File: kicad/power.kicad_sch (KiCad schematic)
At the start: 50 parts, among them J1 Bus_PCI_Express_x1, J2 wago 2060-452/998-404, J3 wago 2060-452/998-404, J4 Conn_01x04, J5 Conn_01x02_Pin, J6 USB_C_Receptacle_USB2.0_16P, Q1 SI7232DN-T1-GE3, U2 RP2040, U4 W25Q128JVP, U9 MCP25625T-E/ML, X1 RP2040 Crystal, Y2 X322516MLB4SI

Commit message: add hierarchical sheets
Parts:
- removed C1: 100u, Capacitor_SMD:C_1210_3225Metric, symbol Device:C
- removed C10, C11: 15p, Capacitor_SMD:C_0402_1005Metric, symbol Device:C
- removed C206, C207, C209, C211, C212, C213, C214, C215, C216, C40, C90, C92, C93: 100n, Capacitor_SMD:C_0402_1005Metric, symbol Device:C
- removed C208, C210: 1u, Capacitor_SMD:C_0402_1005Metric, symbol Device:C
- removed C94, C95: 22p, Capacitor_SMD:C_0402_1005Metric, symbol Device:C
- removed J2, J3: wago 2060-452/998-404, 4in-recovery:wago-2060-452_998-404, symbol recovery:wago-2060-452_998-404
- removed J4: Conn_01x04, Connector_PinHeader_2.54mm:PinHeader_1x04_P2.54mm_Vertical, symbol Connector_Generic:Conn_01x04
- removed J5: Conn_01x02_Pin, Connector_PinHeader_2.54mm:PinHeader_1x02_P2.54mm_Vertical, symbol Connector:Conn_01x02_Pin
- removed Q1: SI7232DN-T1-GE3, 4in-recovery:SI7232DN-T1-GE3, symbol 4in-recovery:SI7232DN-T1-GE3
- removed R12, R30: 1k, Resistor_SMD:R_0402_1005Metric, symbol Device:R
- removed R20, R300: 100, Resistor_SMD:R_0402_1005Metric, symbol Device:R
- removed R203, R204: 27, Resistor_SMD:R_0402_1005Metric, symbol Device:R
- removed R21, R31: 3.3k, Resistor_SMD:R_0402_1005Metric, symbol Device:R
- removed R22, R32: 100k, Resistor_SMD:R_0402_1005Metric, symbol Device:R
- removed R23, R33: 27k, Resistor_SMD:R_0402_1005Metric, symbol Device:R
- removed R91: 10k, Resistor_SMD:R_0402_1005Metric, symbol Device:R
- removed S2: TS-1187A-B-A-B, 4in-kicad-library:TS-1187A-B-A-B, symbol 4in-kicad-library:TS-1187A-B-A-B
- removed U2: RP2040, Package_DFN_QFN:QFN-56-1EP_7x7mm_P0.4mm_EP3.2x3.2mm, symbol MCU_RaspberryPi:RP2040
- removed U4: W25Q128JVP, Package_SON:WSON-8-1EP_6x5mm_P1.27mm_EP3.4x4.3mm, symbol Memory_Flash:W25Q128JVP
- removed U9: MCP25625T-E/ML, 4in-kicad-library:QFN28_6X6MC_MCH, symbol 4in-kicad-library:MCP25625T-E_ML
- removed X1: RP2040 Crystal, 4in-kicad-library:ABM8-272-T3_ABR, symbol 4in-kicad-library:ABM8-272-T3
- removed Y2: X322516MLB4SI, 4in-kicad-library:X322516MLB4SI, symbol 4in-kicad-library:X322516MLB4SI
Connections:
- net VBUS: now reaches J6.A4 (VBUS), J6.A9 (VBUS), J6.B4 (VBUS), J6.B9 (VBUS)
- removed net v_lipo: J1.A16 (VBAT), J1.A17 (VBAT), J1.A18 (VBAT), J1.B16 (VBAT), J1.B17 (VBAT), J1.B18 (VBAT)
- no-connect marks 34 -> 13
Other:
- added sheet digital (digital.kicad_sch)
- added sheet power (analog.kicad_sch)
- note added: "Power Module 0.1.0"
- note removed: "CAN"
- note removed: "CAN Controller/Tranceiver"
- note removed: "Flash"
- note removed: "MCU"
- note removed: "Make sure C210 is close to pin 44 of RP2040"
- note removed: "Make sure C8 is close to pin 45 of RP2040"
- note removed: "Make sure R3 and R4 are close to RP2040"
- note removed: "Parachute Circuit"
- note removed: "RP2040 Crystal"
- note removed: "Recovery Module 0.1.0"
- note removed: "USB Boot shorting headders"
- moved on the sheet: D1, J1, J6, R2, R3, R4

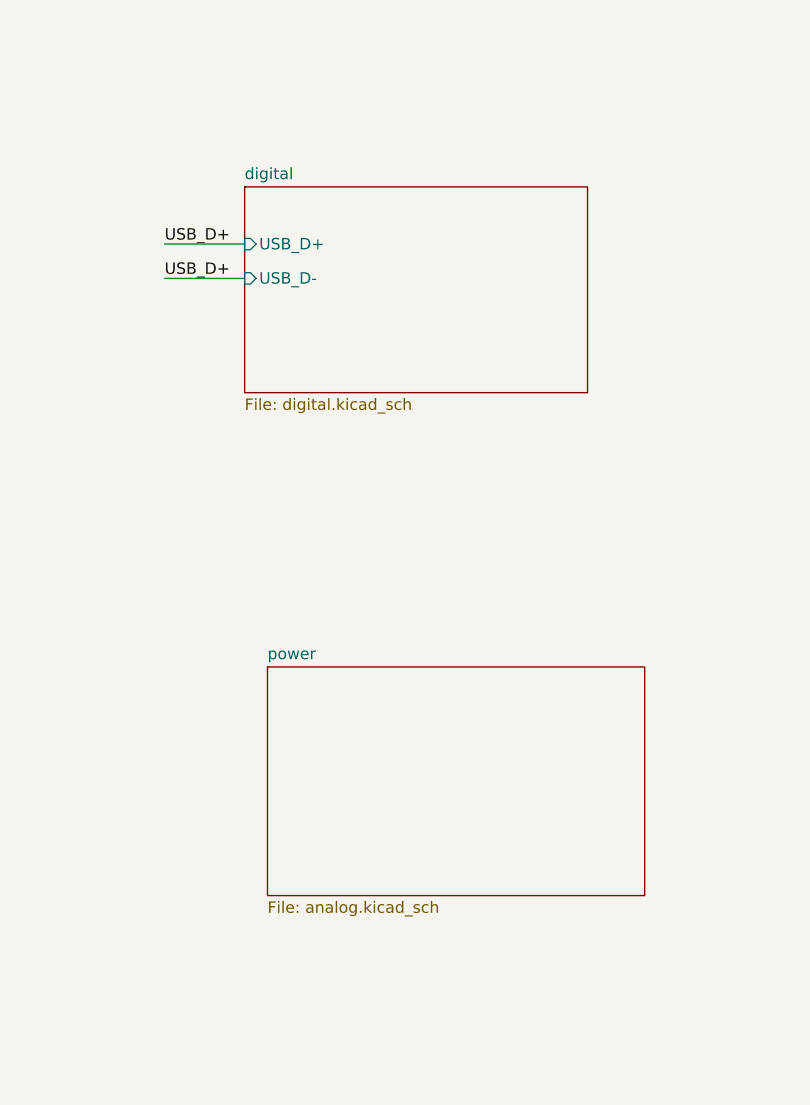
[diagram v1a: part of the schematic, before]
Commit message: add charging/balancing IC to library
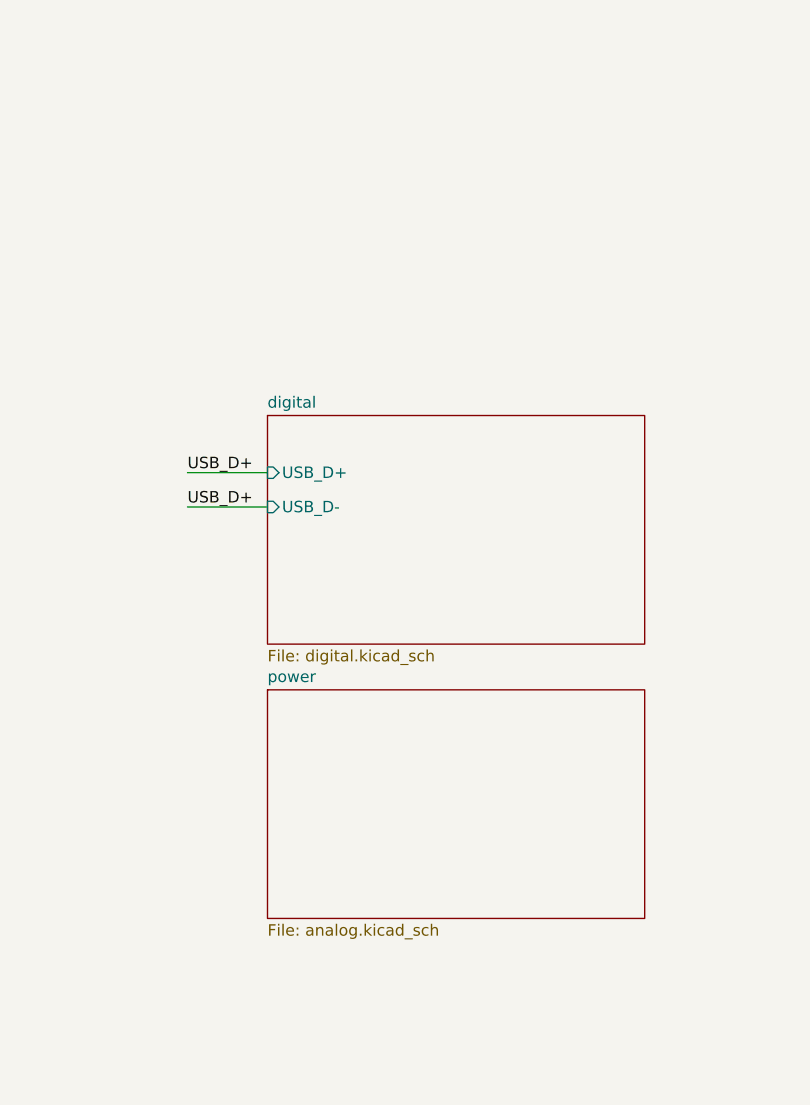
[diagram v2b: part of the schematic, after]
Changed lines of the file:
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@@
+	(wire
+		(pts
+			(xy 199.39 78.74) (xy 208.28 78.74)
+		)
+		(stroke
+			(width 0)
+			(type default)
+		)
+	)
 	(wire
 		(pts
@@
 	(wire
 		(pts
-			(xy 196.85 53.34) (xy 205.74 53.34)
+			(xy 121.92 135.89) (xy 121.92 130.81)
 		)
 		(stroke
@@
 	(wire
 		(pts
-			(xy 121.92 135.89) (xy 121.92 130.81)
+			(xy 121.92 100.33) (xy 121.92 105.41)
 		)
 		(stroke
@@
 	(wire
 		(pts
-			(xy 121.92 100.33) (xy 121.92 105.41)
+			(xy 91.44 105.41) (xy 91.44 110.49)
 		)
 		(stroke
@@
 	(wire
 		(pts
-			(xy 91.44 105.41) (xy 91.44 110.49)
+			(xy 121.92 115.57) (xy 121.92 120.65)
 		)
 		(stroke
@@
 	(wire
 		(pts
-			(xy 121.92 115.57) (xy 121.92 120.65)
+			(xy 91.44 135.89) (xy 91.44 140.97)
 		)
 		(stroke
@@
 	(wire
 		(pts
-			(xy 91.44 135.89) (xy 91.44 140.97)
+			(xy 86.36 156.21) (xy 91.44 156.21)
 		)
 		(stroke
@@
 	(wire
 		(pts
-			(xy 86.36 156.21) (xy 91.44 156.21)
+			(xy 86.36 135.89) (xy 91.44 135.89)
 		)
 		(stroke
@@
 	(wire
 		(pts
-			(xy 86.36 135.89) (xy 91.44 135.89)
+			(xy 127 135.89) (xy 121.92 135.89)
 		)
 		(stroke
@@
 	(wire
 		(pts
-			(xy 127 135.89) (xy 121.92 135.89)
+			(xy 121.92 110.49) (xy 121.92 115.57)
 		)
 		(stroke
@@
 	(wire
 		(pts
-			(xy 121.92 110.49) (xy 121.92 115.57)
+			(xy 91.44 156.21) (xy 91.44 161.29)
 		)
 		(stroke
@@
 	(wire
 		(pts
-			(xy 91.44 156.21) (xy 91.44 161.29)
+			(xy 54.61 55.88) (xy 54.61 58.42)
 		)
 		(stroke
@@
 	(wire
 		(pts
-			(xy 54.61 55.88) (xy 54.61 58.42)
+			(xy 199.39 74.93) (xy 208.28 74.93)
 		)
 		(stroke
@@
 		(pts
 			(xy 127 156.21) (xy 121.92 156.21)
-		)
-		(stroke
-			(width 0)
-			(type default)
-		)
-	)
-	(wire
-		(pts
-			(xy 196.85 49.53) (xy 205.74 49.53)
 		)
 		(stroke
@@
 	)
 	(label "USB_D+"
-		(at 196.85 49.53 0)
+		(at 199.39 74.93 0)
 		(effects
 			(font
@@
 	)
 	(label "USB_D+"
-		(at 196.85 53.34 0)
+		(at 199.39 78.74 0)
 		(effects
 			(font
@@
 	)
 	(sheet
-		(at 205.74 43.18)
-		(size 38.1 22.86)
-		(exclude_from_sim no)
-		(in_bom yes)
-		(on_board yes)
-		(dnp no)
-		(fields_autoplaced yes)
-		(stroke
-			(width 0.1524)
-			(type solid)
-		)
-		(fill
-			(color 0 0 0 0.0000)
-		)
-		(property "Sheetname" "digital"
-			(at 205.74 42.4684 0)
-			(effects
-				(font
-					(size 1.27 1.27)
-				)
-				(justify left bottom)
-			)
-		)
-		(property "Sheetfile" "digital.kicad_sch"
-			(at 205.74 66.6246 0)
-			(effects
-				(font
-					(size 1.27 1.27)
-				)
-				(justify left top)
-			)
-		)
-		(pin "USB_D+" input
-			(at 205.74 49.53 180)
-			(effects
-				(font
-					(size 1.27 1.27)
-				)
-				(justify left)
-			)
-		)
-		(pin "USB_D-" input
-			(at 205.74 53.34 180)
-			(effects
-				(font
-					(size 1.27 1.27)
-				)
-				(justify left)
-			)
-		)
-		(instances
-			(project "power"
-				(path "/612ece3f-e722-4b33-8111-645d24cfcf05"
-					(page "2")
-				)
-			)
-		)
-	)
-	(sheet
-		(at 208.28 96.52)
+		(at 208.28 68.58)
 		(size 41.91 25.4)
 		(exclude_from_sim no)
@@
 			(color 0 0 0 0.0000)
 		)
+		(property "Sheetname" "digital"
+			(at 208.28 67.8684 0)
+			(effects
+				(font
+					(size 1.27 1.27)
+				)
+				(justify left bottom)
+			)
+		)
+		(property "Sheetfile" "digital.kicad_sch"
+			(at 208.28 94.5646 0)
+			(effects
+				(font
+					(size 1.27 1.27)
+				)
+				(justify left top)
+			)
+		)
+		(pin "USB_D+" input
+			(at 208.28 74.93 180)
+			(effects
+				(font
+					(size 1.27 1.27)
+				)
+				(justify left)
+			)
+		)
+		(pin "USB_D-" input
+			(at 208.28 78.74 180)
+			(effects
+				(font
+					(size 1.27 1.27)
+				)
+				(justify left)
+			)
+		)
+		(instances
+			(project "power"
+				(path "/612ece3f-e722-4b33-8111-645d24cfcf05"
+					(page "2")
+				)
+			)
+		)
+	)
+	(sheet
+		(at 208.28 99.06)
+		(size 41.91 25.4)
+		(exclude_from_sim no)
+		(in_bom yes)
+		(on_board yes)
+		(dnp no)
+		(fields_autoplaced yes)
+		(stroke
+			(width 0.1524)
+			(type solid)
+		)
+		(fill
+			(color 0 0 0 0.0000)
+		)
 		(property "Sheetname" "power"
-			(at 208.28 95.8084 0)
+			(at 208.28 98.3484 0)
 			(effects
 				(font
@@
 		)
 		(property "Sheetfile" "analog.kicad_sch"
-			(at 208.28 122.5046 0)
-			(effects
-				(font
+			(at 208.28 125.0446 0)
+			(effects
+				(font

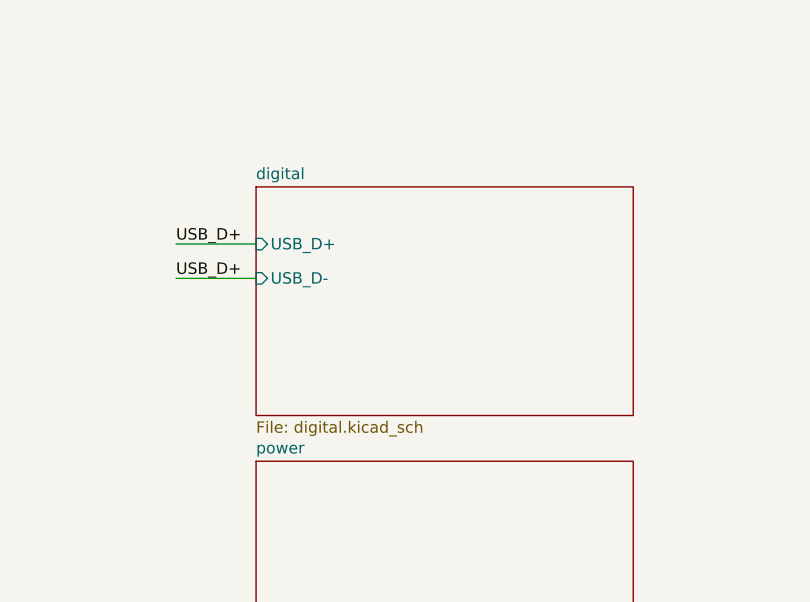
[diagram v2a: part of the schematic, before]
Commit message: update library schmatic for balancing IC
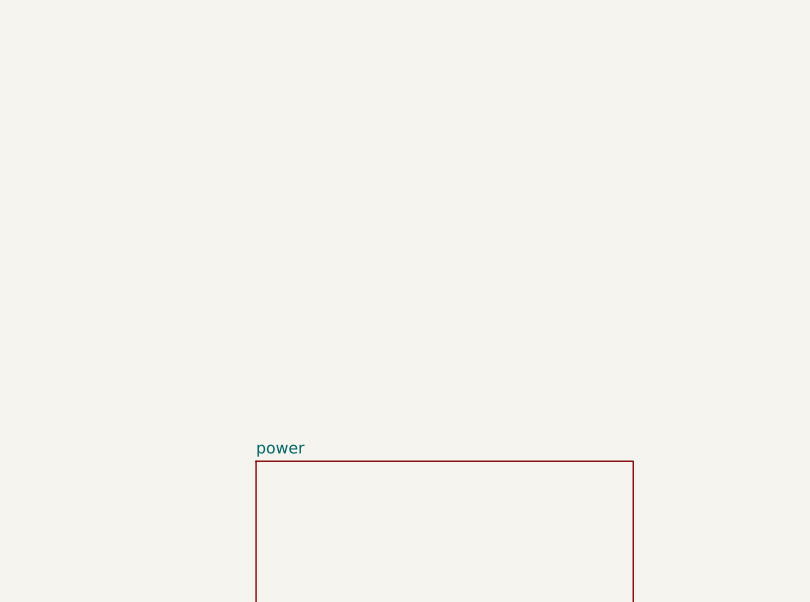
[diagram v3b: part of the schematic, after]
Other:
- removed sheet digital
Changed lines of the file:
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@@
 	(wire
 		(pts
-			(xy 199.39 78.74) (xy 208.28 78.74)
+			(xy 91.44 110.49) (xy 91.44 115.57)
 		)
 		(stroke
@@
 	(wire
 		(pts
-			(xy 91.44 110.49) (xy 91.44 115.57)
+			(xy 121.92 105.41) (xy 121.92 110.49)
 		)
 		(stroke
@@
 	(wire
 		(pts
-			(xy 121.92 105.41) (xy 121.92 110.49)
+			(xy 54.61 53.34) (xy 54.61 50.8)
 		)
 		(stroke
@@
 	(wire
 		(pts
-			(xy 54.61 53.34) (xy 54.61 50.8)
+			(xy 121.92 156.21) (xy 121.92 151.13)
 		)
 		(stroke
@@
 	(wire
 		(pts
-			(xy 121.92 156.21) (xy 121.92 151.13)
+			(xy 91.44 135.89) (xy 91.44 130.81)
 		)
 		(stroke
@@
 	(wire
 		(pts
-			(xy 91.44 135.89) (xy 91.44 130.81)
+			(xy 121.92 135.89) (xy 121.92 130.81)
 		)
 		(stroke
@@
 	(wire
 		(pts
-			(xy 121.92 135.89) (xy 121.92 130.81)
+			(xy 121.92 100.33) (xy 121.92 105.41)
 		)
 		(stroke
@@
 	(wire
 		(pts
-			(xy 121.92 100.33) (xy 121.92 105.41)
+			(xy 91.44 105.41) (xy 91.44 110.49)
 		)
 		(stroke
@@
 	(wire
 		(pts
-			(xy 91.44 105.41) (xy 91.44 110.49)
+			(xy 121.92 115.57) (xy 121.92 120.65)
 		)
 		(stroke
@@
 	(wire
 		(pts
-			(xy 121.92 115.57) (xy 121.92 120.65)
+			(xy 91.44 135.89) (xy 91.44 140.97)
 		)
 		(stroke
@@
 	(wire
 		(pts
-			(xy 91.44 135.89) (xy 91.44 140.97)
+			(xy 86.36 156.21) (xy 91.44 156.21)
 		)
 		(stroke
@@
 	(wire
 		(pts
-			(xy 86.36 156.21) (xy 91.44 156.21)
+			(xy 86.36 135.89) (xy 91.44 135.89)
 		)
 		(stroke
@@
 	(wire
 		(pts
-			(xy 86.36 135.89) (xy 91.44 135.89)
+			(xy 127 135.89) (xy 121.92 135.89)
 		)
 		(stroke
@@
 	(wire
 		(pts
-			(xy 127 135.89) (xy 121.92 135.89)
+			(xy 121.92 110.49) (xy 121.92 115.57)
 		)
 		(stroke
@@
 	(wire
 		(pts
-			(xy 121.92 110.49) (xy 121.92 115.57)
+			(xy 91.44 156.21) (xy 91.44 161.29)
 		)
 		(stroke
@@
 	(wire
 		(pts
-			(xy 91.44 156.21) (xy 91.44 161.29)
-		)
-		(stroke
-			(width 0)
-			(type default)
-		)
-	)
-	(wire
-		(pts
 			(xy 54.61 55.88) (xy 54.61 58.42)
-		)
-		(stroke
-			(width 0)
-			(type default)
-		)
-	)
-	(wire
-		(pts
-			(xy 199.39 74.93) (xy 208.28 74.93)
 		)
 		(stroke
@@
 	)
 	(label "USB_D+"
-		(at 199.39 74.93 0)
-		(effects
-			(font
-				(size 1.27 1.27)
-			)
-			(justify left bottom)
-		)
-	)
-	(label "USB_D+"
 		(at 54.61 58.42 0)
-		(effects
-			(font
-				(size 1.27 1.27)
-			)
-			(justify left bottom)
-		)
-	)
-	(label "USB_D+"
-		(at 199.39 78.74 0)
 		(effects
 			(font
@@
 				)
 			)
-		)
-	)
-	(sheet
-		(at 208.28 68.58)
-		(size 41.91 25.4)
-		(exclude_from_sim no)
-		(in_bom yes)
-		(on_board yes)
-		(dnp no)
-		(fields_autoplaced yes)
-		(stroke
-			(width 0.1524)
-			(type solid)
-		)
-		(fill
-			(color 0 0 0 0.0000)
-		)
-		(property "Sheetname" "digital"
-			(at 208.28 67.8684 0)
-			(effects
-				(font
-					(size 1.27 1.27)
-				)
-				(justify left bottom)
-			)
-		)
-		(property "Sheetfile" "digital.kicad_sch"
-			(at 208.28 94.5646 0)
-			(effects
-				(font
-					(size 1.27 1.27)
-				)
-				(justify left top)
-			)
-		)
-		(pin "USB_D+" input
-			(at 208.28 74.93 180)
-			(effects
-				(font
-					(size 1.27 1.27)
-				)
-				(justify left)
-			)
-		)
-		(pin "USB_D-" input
-			(at 208.28 78.74 180)
-			(effects
-				(font
-					(size 1.27 1.27)
-				)
-				(justify left)
-			)
-		)
-		(instances
-			(project "power"
-				(path "/612ece3f-e722-4b33-8111-645d24cfcf05"
-					(page "2")
-				)
-			)

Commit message: update anotations
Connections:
- net CANH: no longer names the net of J1.A1 (CANH)
- net CANL: no longer names the net of J1.A3 (CANN)
- net USB_D+: no longer names the net of J6.A6 (D+)
- net USB_D+: no longer J6.B6 (D+)
- net USB_D-: no longer names the net of J6.A7 (D-)
- net USB_D-: no longer J6.B7 (D-)
- no-connect marks 13 -> 19
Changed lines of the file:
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@@
+	)
+	(no_connect
+		(at 91.44 90.17)
 	)
 	(no_connect
@@
 	)
 	(no_connect
+		(at 54.61 58.42)
+	)
+	(no_connect
 		(at 121.92 181.61)
 	)
@@
 	)
 	(no_connect
+		(at 91.44 100.33)
+	)
+	(no_connect
 		(at 91.44 125.73)
+	)
+	(no_connect
+		(at 54.61 50.8)
+	)
+	(no_connect
+		(at 54.61 55.88)
+	)
+	(no_connect
+		(at 54.61 53.34)
 	)
 	(no_connect
@@
 	(wire
 		(pts
-			(xy 54.61 53.34) (xy 54.61 50.8)
+			(xy 121.92 156.21) (xy 121.92 151.13)
 		)
 		(stroke
@@
 	(wire
 		(pts
-			(xy 121.92 156.21) (xy 121.92 151.13)
+			(xy 91.44 135.89) (xy 91.44 130.81)
 		)
 		(stroke
@@
 	(wire
 		(pts
-			(xy 91.44 135.89) (xy 91.44 130.81)
+			(xy 121.92 135.89) (xy 121.92 130.81)
 		)
 		(stroke
@@
 	(wire
 		(pts
-			(xy 121.92 135.89) (xy 121.92 130.81)
+			(xy 121.92 100.33) (xy 121.92 105.41)
 		)
 		(stroke
@@
 	(wire
 		(pts
-			(xy 121.92 100.33) (xy 121.92 105.41)
+			(xy 91.44 105.41) (xy 91.44 110.49)
 		)
 		(stroke
@@
 	(wire
 		(pts
-			(xy 91.44 105.41) (xy 91.44 110.49)
+			(xy 121.92 115.57) (xy 121.92 120.65)
 		)
 		(stroke
@@
 	(wire
 		(pts
-			(xy 121.92 115.57) (xy 121.92 120.65)
+			(xy 91.44 135.89) (xy 91.44 140.97)
 		)
 		(stroke
@@
 	(wire
 		(pts
-			(xy 91.44 135.89) (xy 91.44 140.97)
+			(xy 86.36 156.21) (xy 91.44 156.21)
 		)
 		(stroke
@@
 	(wire
 		(pts
-			(xy 86.36 156.21) (xy 91.44 156.21)
+			(xy 86.36 135.89) (xy 91.44 135.89)
 		)
 		(stroke
@@
 	(wire
 		(pts
-			(xy 86.36 135.89) (xy 91.44 135.89)
+			(xy 127 135.89) (xy 121.92 135.89)
 		)
 		(stroke
@@
 	(wire
 		(pts
-			(xy 127 135.89) (xy 121.92 135.89)
+			(xy 121.92 110.49) (xy 121.92 115.57)
 		)
 		(stroke
@@
 	(wire
 		(pts
-			(xy 121.92 110.49) (xy 121.92 115.57)
+			(xy 91.44 156.21) (xy 91.44 161.29)
 		)
 		(stroke
@@
 	(wire
 		(pts
-			(xy 91.44 156.21) (xy 91.44 161.29)
+			(xy 121.92 95.25) (xy 121.92 100.33)
 		)
 		(stroke
@@
 	(wire
 		(pts
-			(xy 54.61 55.88) (xy 54.61 58.42)
+			(xy 127 156.21) (xy 121.92 156.21)
 		)
 		(stroke
@@
 	(wire
 		(pts
-			(xy 121.92 95.25) (xy 121.92 100.33)
+			(xy 91.44 115.57) (xy 91.44 120.65)
 		)
 		(stroke
@@
 	(wire
 		(pts
-			(xy 127 156.21) (xy 121.92 156.21)
+			(xy 157.48 135.89) (xy 157.48 138.43)
 		)
 		(stroke
@@
 	(wire
 		(pts
-			(xy 91.44 115.57) (xy 91.44 120.65)
+			(xy 157.48 156.21) (xy 157.48 153.67)
 		)
 		(stroke
@@
 	(wire
 		(pts
-			(xy 157.48 135.89) (xy 157.48 138.43)
+			(xy 121.92 90.17) (xy 121.92 95.25)
 		)
 		(stroke
@@
 	(wire
 		(pts
-			(xy 157.48 156.21) (xy 157.48 153.67)
+			(xy 91.44 156.21) (xy 91.44 151.13)
 		)
 		(stroke
@@
 	(wire
 		(pts
-			(xy 121.92 90.17) (xy 121.92 95.25)
+			(xy 121.92 156.21) (xy 121.92 161.29)
 		)
 		(stroke
 			(width 0)
 			(type default)
-		)
-	)
-	(wire
-		(pts
-			(xy 91.44 156.21) (xy 91.44 151.13)
-		)
-		(stroke
-			(width 0)
-			(type default)
-		)
-	)
-	(wire
-		(pts
-			(xy 121.92 156.21) (xy 121.92 161.29)
-		)
-		(stroke
-			(width 0)
-			(type default)
-		)
-	)
-	(label "USB_D-"
-		(at 54.61 53.34 0)
-		(effects
-			(font
-				(size 1.27 1.27)
-			)
-			(justify left bottom)
 		)
 	)
@@
 			)
 			(justify left bottom)
-		)
-	)
-	(label "USB_D+"
-		(at 54.61 58.42 0)
-		(effects
-			(font
-				(size 1.27 1.27)
-			)
-			(justify left bottom)
-		)
-	)
-	(global_label "CANL"
-		(shape bidirectional)
-		(at 91.44 100.33 180)
-		(fields_autoplaced yes)
-		(effects
-			(font
-				(size 1.27 1.27)
-			)
-			(justify right)
-		)
-		(property "Intersheetrefs" "${INTERSHEET_REFS}"
-			(at 82.6263 100.33 0)
-			(effects
-				(font
-					(size 1.27 1.27)
-				)
-				(justify right)
-				(hide yes)
-			)
-		)
-	)
-	(global_label "CANH"
-		(shape bidirectional)
-		(at 91.44 90.17 180)
-		(fields_autoplaced yes)
-		(effects
-			(font
-				(size 1.27 1.27)
-			)
-			(justify right)
-		)
-		(property "Intersheetrefs" "${INTERSHEET_REFS}"
-			(at 82.3239 90.17 0)
-			(effects
-				(font
-					(size 1.27 1.27)
-				)
-				(justify right)
-				(hide yes)
-			)
 		)
 	)
@@
 	)
 	(sheet
-		(at 208.28 99.06)
+		(at 189.23 69.85)
 		(size 41.91 25.4)
 		(exclude_from_sim no)
@@
 		)
 		(property "Sheetname" "power"
-			(at 208.28 98.3484 0)
+			(at 189.23 69.1384 0)
 			(effects
 				(font
@@
 		)
 		(property "Sheetfile" "analog.kicad_sch"
-			(at 208.28 125.0446 0)
-			(effects
-				(font
+			(at 189.23 95.8346 0)
+			(effects
+				(font

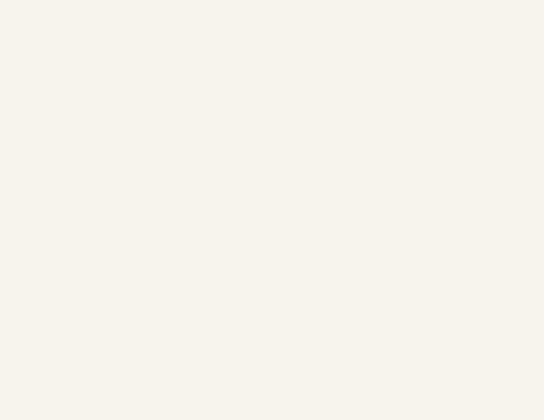
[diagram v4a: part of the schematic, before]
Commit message: add MB30 connector
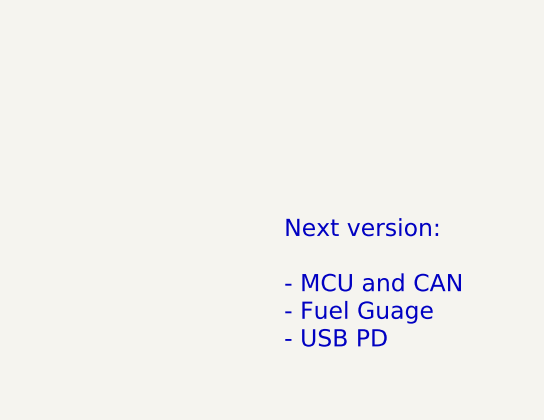
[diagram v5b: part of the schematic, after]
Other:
- note added: "Next version: - MCU and CAN - Fuel Guage - USB PD"
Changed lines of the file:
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@@
+		)
+	)
+	(text "Next version:\n\n- MCU and CAN\n- Fuel Guage\n- USB PD"
+		(exclude_from_sim no)
+		(at 301.752 175.768 0)
+		(effects
+			(font
+				(size 1.905 1.905)
+			)
+			(justify left)
 		)
 	)
